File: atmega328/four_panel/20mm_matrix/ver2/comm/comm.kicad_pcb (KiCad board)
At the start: 2 copper layers, 40 x 40 mm, 12 parts, among them IC5 ATMEGA328-A, P1 CONN15, P2 CONN15, P4 CONN_2X2, P5 CONN_2X2, P6 CONN_2X2, P7 CONN_2X2, X5 CER_RESO

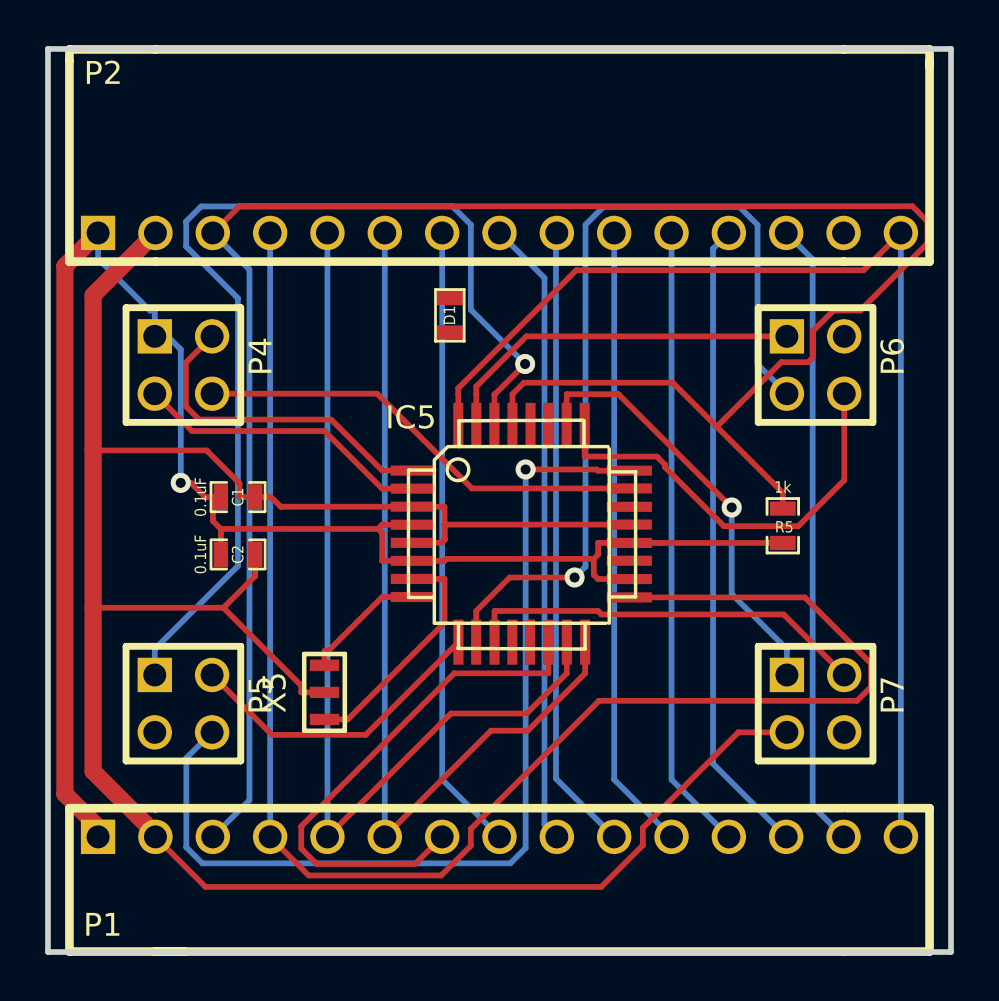
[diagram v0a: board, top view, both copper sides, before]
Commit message: Worked on ver2 of atmega328 4x20mm driver and comm pcbs.
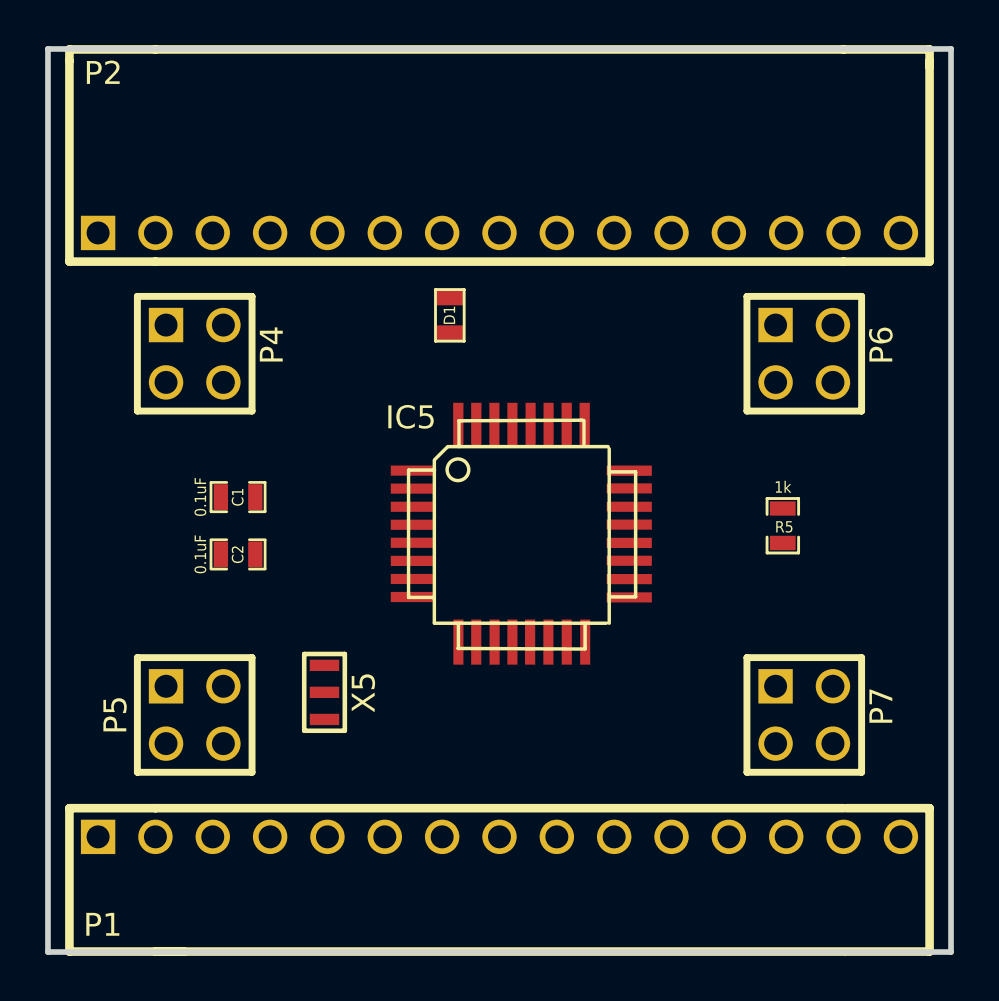
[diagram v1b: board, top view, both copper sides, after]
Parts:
- moved P4 0.71 mm to (56.5, 63.5)
- moved P5 0.71 mm to (56.5, 79.5)
- moved P6 0.71 mm to (83.5, 63.5)
- moved P7 0.71 mm to (83.5, 79.5)
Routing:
- net GND: track 104.2 -> 0.00 mm
- net /RESET_MSTR: track 91.2 -> 0.00 mm
- net +5V: track 76.8 -> 0.00 mm, vias 1 -> 0
- net /B0_SCK: track 70.9 -> 0.00 mm
- net /EXT_INT0: track 50.9 -> 0.00 mm
- net /B1_MISO: track 46.2 -> 0.00 mm, vias 1 -> 0
- net /RESET_DRV1: track 42.6 -> 0.00 mm, vias 1 -> 0
- net /B0_MOSI: track 41.7 -> 0.00 mm
- net /B0_MISO: track 40.0 -> 0.00 mm
- net /B1_CS2: track 38.5 -> 0.00 mm, vias 1 -> 0
- net /B0_CS6: track 28.4 -> 0.00 mm
- net /B0_CS3: track 27.8 -> 0.00 mm
- net /B0_CS2: track 27.8 -> 0.00 mm
- net /B0_CS4: track 27.8 -> 0.00 mm
- net /B0_CS1: track 27.8 -> 0.00 mm
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
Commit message: Added ground pin header to backside of ver 2 com pcb.
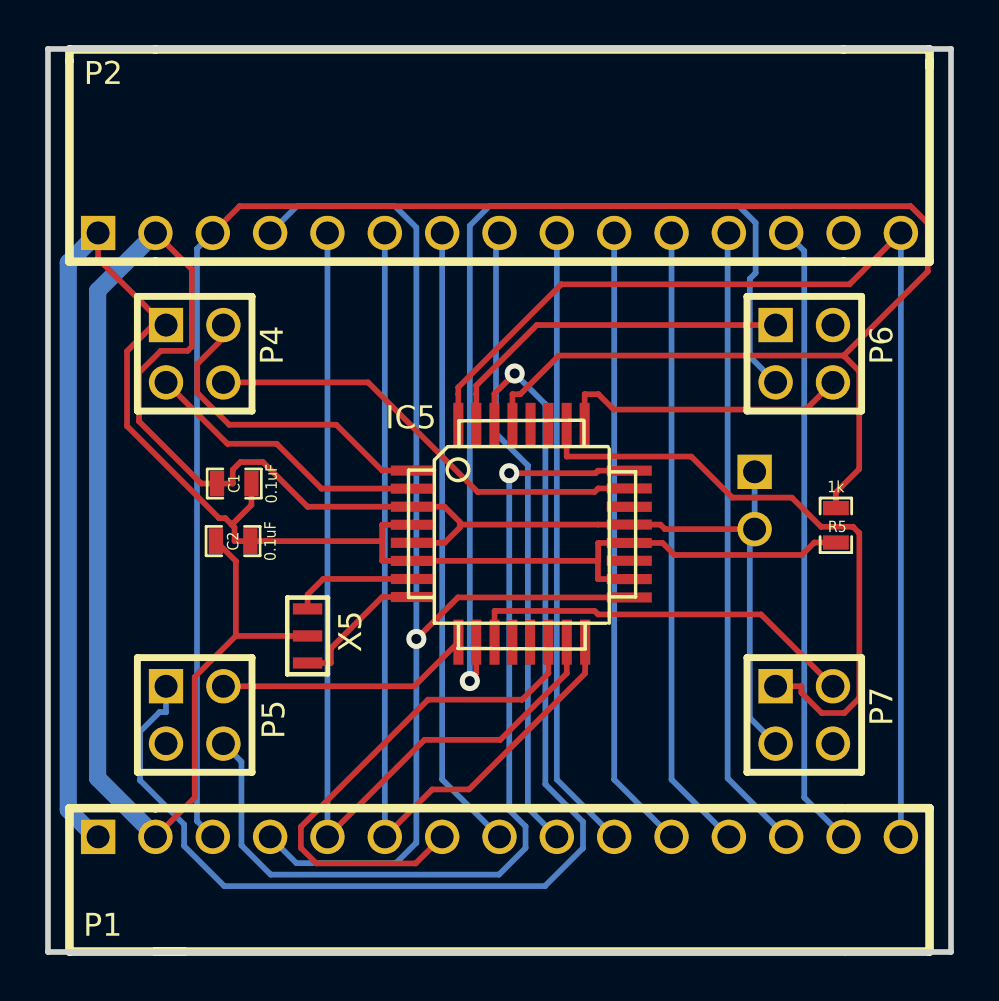
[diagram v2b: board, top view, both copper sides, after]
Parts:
- removed D1: DIODE, SM0603
- added P8: CONN_2, RT_ANG_2PIN, B.Cu at (81.3, 70.0)
- moved X5 2.61 mm to (61.5, 76.0), turned to 270 degrees
- moved R5 2.35 mm to (84.9, 71.1)
- moved C2 0.63 mm to (58.2, 71.8), turned to 180 degrees
- moved C1 0.62 mm to (58.2, 69.2), turned to 180 degrees
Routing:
- net GND: track 0.00 -> 103.2 mm
- net /RESET_MSTR: track 0.00 -> 91.4 mm
- net +5V: track 0.00 -> 81.0 mm
- net /B1_MISO: track 0.00 -> 52.6 mm, vias 0 -> 1
- net /B0_SCK: track 0.00 -> 52.1 mm, vias 0 -> 1
- net /EXT_INT0: track 0.00 -> 50.9 mm
- net /B1_CS2: track 0.00 -> 43.0 mm, vias 0 -> 1
- net /B0_MOSI: track 0.00 -> 41.7 mm
- net /RESET_DRV1: track 0.00 -> 40.7 mm, vias 0 -> 1
- net /B0_MISO: track 0.00 -> 40.0 mm
- net /B0_CS2: track 0.00 -> 27.9 mm
- net /B0_CS6: track 0.00 -> 27.8 mm
- net /B0_CS4: track 0.00 -> 27.8 mm
- net /B0_CS1: track 0.00 -> 27.8 mm
- net /B0_CS5: track 0.00 -> 27.8 mm
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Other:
- board text added: "4-Matrix Atmega328 Comm v0.2 www.iorodeo.com"
- board text removed: "4-Matrix Atmega328 Comm v0.1 www.iorodeo.com"

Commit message: Adde ground holes to 4x20mm atmega328 comm
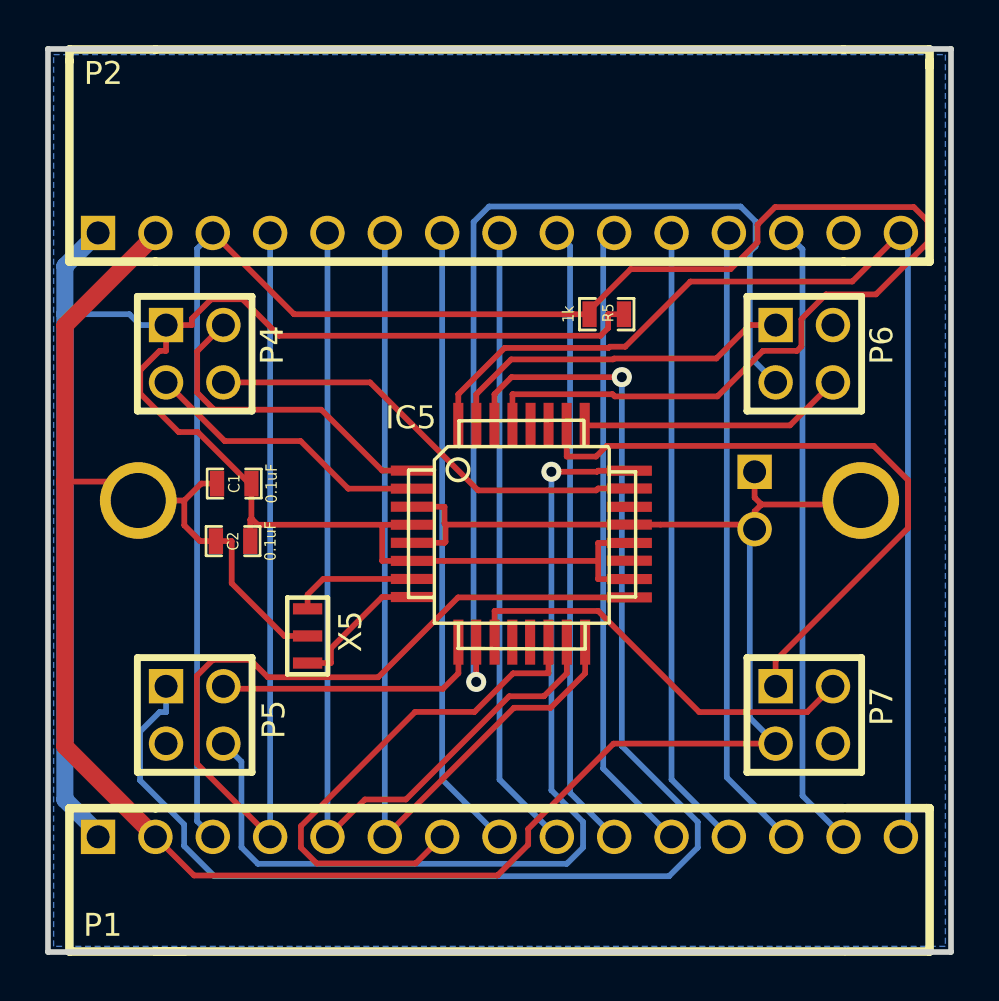
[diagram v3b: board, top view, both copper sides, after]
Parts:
- added M1: CONN_1, 2-56 Mount Holes, F.Cu at (54.0, 70.0)
- added M2: CONN_1, 2-56 Mount Holes, F.Cu at (86.0, 70.0)
- moved R5 13.8 mm to (74.8, 61.8), turned to 0 degrees
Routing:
- net GND: track 103.2 -> 113.6 mm
- net +5V: track 81.0 -> 90.7 mm
- net /B1_MISO: track 52.6 -> 61.9 mm
- net /B0_SCK: track 52.1 -> 56.5 mm, vias 1 -> 0
- net /RESET_MSTR: track 91.4 -> 87.6 mm
- net /RESET_DRV2: track 13.2 -> 11.8 mm
- net /RESET_DRV3: track 27.7 -> 28.9 mm
- net /B2_CS3: track 17.8 -> 18.7 mm
- net /B1_CS1: track 11.2 -> 12.1 mm
- net /RESET_DRV1: track 40.7 -> 41.4 mm
- added copper zone on B.Cu, net GND
